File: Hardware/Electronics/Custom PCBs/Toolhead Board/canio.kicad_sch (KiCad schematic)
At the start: 11 parts, among them J1 120TR, J3 CAN, U6 SN65HVD1050D

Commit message: some updates
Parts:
- C18, C19, C22: footprint Capacitor_SMD:C_0402_1005Metric -> (none)
- C23, C24: footprint Capacitor_SMD:C_0402_1005Metric -> (none); LCSC C881999 -> (none)
- CR1: footprint Package_TO_SOT_SMD:SOT-23 -> (none)
- J1: footprint Connector_PinHeader_2.54mm:PinHeader_1x02_P2.54mm_Vertical -> (none)
- J3: footprint Connector_JST:JST_PH_S4B-PH-K_1x04_P2.00mm_Horizontal -> (none)
- R8, R9: footprint Resistor_SMD:R_0402_1005Metric -> (none); LCSC C966873 -> (none)
- U6: footprint Package_SO:SOIC-8_3.9x4.9mm_P1.27mm -> (none)

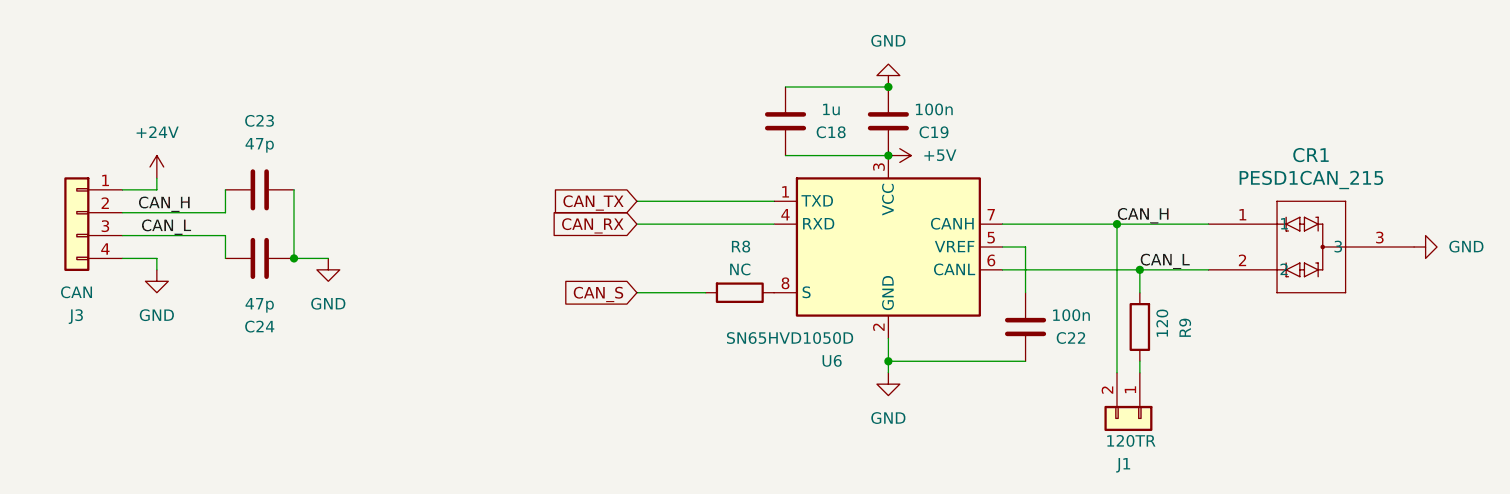
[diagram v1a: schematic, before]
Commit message: Finish Toolhead Schematic
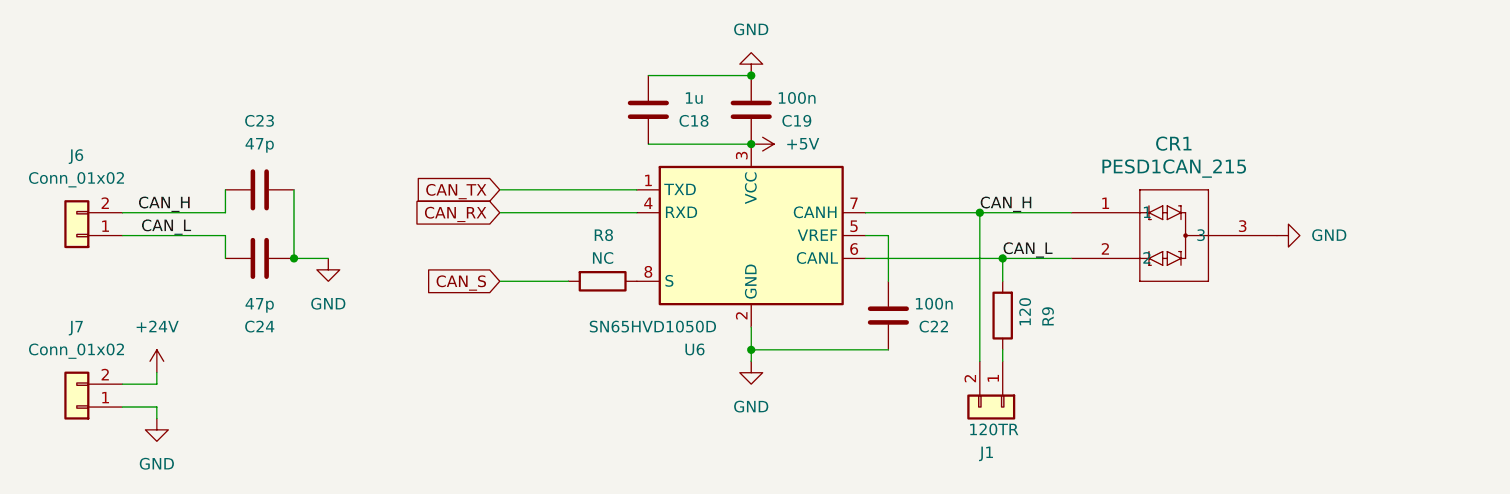
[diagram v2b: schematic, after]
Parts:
- removed J3: CAN, symbol Connector_Generic:Conn_01x04
- added J6, J7: Conn_01x02, symbol Connector_Generic:Conn_01x02
- C18: Digikey (none) -> 1276-1102-1-ND
- C19, C22: Digikey (none) -> 1276-1935-1-ND
- C23, C24: Digikey (none) -> 311-4037-1-ND
- CR1: Digikey (none) -> 5272-PESD1CANCT-ND
- J1: Digikey (none) -> 732-5315-ND
- R8: footprint (none) -> Resistor_SMD:R_0603_1608Metric_Pad0.98x0.95mm_HandSolder
- R9: footprint (none) -> Resistor_SMD:R_0603_1608Metric_Pad0.98x0.95mm_HandSolder; Digikey (none) -> RMCF0603FT120RCT-ND
- U6: Digikey (none) -> 296-19416-5-ND
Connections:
- net +24V: now also J7.2 (Pin_2)
- net CAN_H: now also J6.2 (Pin_2)
- net CAN_L: now also J6.1 (Pin_1)
- net GND: now also J7.1 (Pin_1)
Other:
- moved on the sheet: C18, C19, C22, CR1, J1, R8, R9, U6

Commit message: Updated Footprints
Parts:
- C19: renamed from C18; footprint (none) -> Capacitor_SMD:C_0603_1608Metric_Pad1.08x0.95mm_HandSolder
- C20: renamed from C19; footprint (none) -> Capacitor_SMD:C_0603_1608Metric_Pad1.08x0.95mm_HandSolder
- C23: renamed from C22; footprint (none) -> Capacitor_SMD:C_0603_1608Metric_Pad1.08x0.95mm_HandSolder
- renumbered C23 to C21, C24 to C22, J1 to J8, R8 to R10, R9 to R11, U6 to U5

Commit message: Continue adding footprints
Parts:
- C21, C22: footprint (none) -> Capacitor_SMD:C_0603_1608Metric_Pad1.08x0.95mm_HandSolder
- CR1: footprint (none) -> Package_TO_SOT_SMD:SOT-23
- J6, J7: footprint (none) -> Connector_JST:JST_XH_B2B-XH-AM_1x02_P2.50mm_Vertical
- J8: footprint (none) -> Connector_PinHeader_2.54mm:PinHeader_1x02_P2.54mm_Vertical
- U5: footprint (none) -> Package_SO:SOIC-8_3.9x4.9mm_P1.27mm
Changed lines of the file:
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@@
 			)
 		)
-		(property "Footprint" ""
+		(property "Footprint" "Connector_PinHeader_2.54mm:PinHeader_1x02_P2.54mm_Vertical"
 			(at 130.81 59.69 0)
 			(effects
@@
 			)
 		)
-		(property "Footprint" ""
+		(property "Footprint" "Connector_JST:JST_XH_B2B-XH-AM_1x02_P2.50mm_Vertical"
 			(at 27.94 40.64 0)
 			(effects
@@
 			)
 		)
-		(property "Footprint" ""
+		(property "Footprint" "Capacitor_SMD:C_0603_1608Metric_Pad1.08x0.95mm_HandSolder"
 			(at 52.07 44.1452 0)
 			(effects
@@
 			)
 		)
-		(property "Footprint" ""
+		(property "Footprint" "Package_SO:SOIC-8_3.9x4.9mm_P1.27mm"
 			(at 102.87 53.34 0)
 			(effects
@@
 			)
 		)
-		(property "Footprint" ""
+		(property "Footprint" "Capacitor_SMD:C_0603_1608Metric_Pad1.08x0.95mm_HandSolder"
 			(at 52.07 34.5948 0)
 			(effects
@@
 			)
 		)
-		(property "Footprint" ""
+		(property "Footprint" "Connector_JST:JST_XH_B2B-XH-AM_1x02_P2.50mm_Vertical"
 			(at 27.94 59.69 0)
 			(effects
@@
 			)
 		)
-		(property "Footprint" ""
+		(property "Footprint" "Package_TO_SOT_SMD:SOT-23"
 			(at 138.43 38.1 0)
 			(effects

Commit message: Get basic Toolhead Board outline
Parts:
- renumbered J6 to J10, J7 to J11, J8 to J12
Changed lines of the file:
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@@
 		(on_board yes)
 		(dnp no)
-		(property "Reference" "J8"
+		(property "Reference" "J12"
 			(at 128.27 64.77 90)
 			(effects
@@
 			(project "Toolhead Board"
 				(path "/a1747683-152e-4245-ab61-2d33ce6021ef/ddf7d789-b89f-4838-a0de-61c290d748de"
-					(reference "J8")
+					(reference "J12")
 					(unit 1)
 				)
@@
 		(dnp no)
 		(fields_autoplaced yes)
-		(property "Reference" "J6"
+		(property "Reference" "J10"
 			(at 27.94 31.75 0)
 			(effects
@@
 			(project "Toolhead Board"
 				(path "/a1747683-152e-4245-ab61-2d33ce6021ef/ddf7d789-b89f-4838-a0de-61c290d748de"
-					(reference "J6")
+					(reference "J10")
 					(unit 1)
 				)
@@
 		(dnp no)
 		(fields_autoplaced yes)
-		(property "Reference" "J7"
+		(property "Reference" "J11"
 			(at 27.94 50.8 0)
 			(effects
@@
 			(project "Toolhead Board"
 				(path "/a1747683-152e-4245-ab61-2d33ce6021ef/ddf7d789-b89f-4838-a0de-61c290d748de"
-					(reference "J7")
-					(unit 1)
-				)
+					(reference "J11")
+					(unit 1)
+				)

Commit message: Update layout
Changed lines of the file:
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@@
+	(wire
+		(pts
+			(xy 130.81 43.18) (xy 130.81 45.72)
+		)
+		(stroke
+			(width 0)
+			(type default)
+		)
+	)
+	(wire
+		(pts
+			(xy 44.45 40.64) (xy 33.02 40.64)
+		)
+		(stroke
+			(width 0)
+			(type default)
+		)
+	)
 	(wire
 		(pts
@@
 	(wire
 		(pts
-			(xy 130.81 43.18) (xy 130.81 45.72)
-		)
-		(stroke
-			(width 0)
-			(type default)
-		)
-	)
-	(wire
-		(pts
 			(xy 118.11 40.64) (xy 115.57 40.64)
 		)
@@
 	(wire
 		(pts
-			(xy 33.02 40.64) (xy 44.45 40.64)
-		)
-		(stroke
-			(width 0)
-			(type default)
-		)
-	)
-	(wire
-		(pts
 			(xy 44.45 35.56) (xy 44.45 38.1)
 		)
@@
 		)
 	)
-	(label "CAN_L"
-		(at 40.64 40.64 180)
-		(fields_autoplaced yes)
-		(effects
-			(font
-				(size 1.27 1.27)
-			)
-			(justify right bottom)
-		)
-	)
-	(label "CAN_H"
-		(at 128.27 38.1 0)
-		(fields_autoplaced yes)
-		(effects
-			(font
-				(size 1.27 1.27)
-			)
-			(justify left bottom)
-		)
-	)
-	(label "CAN_H"
-		(at 40.64 38.1 180)
-		(fields_autoplaced yes)
-		(effects
-			(font
-				(size 1.27 1.27)
-			)
-			(justify right bottom)
-		)
-	)
-	(label "CAN_L"
-		(at 130.81 43.18 0)
-		(fields_autoplaced yes)
-		(effects
-			(font
-				(size 1.27 1.27)
-			)
-			(justify left bottom)
+	(global_label "CAN_L"
+		(shape input)
+		(at 44.45 43.18 270)
+		(fields_autoplaced yes)
+		(effects
+			(font
+				(size 1.27 1.27)
+			)
+			(justify right)
+		)
+		(property "Intersheetrefs" "${INTERSHEET_REFS}"
+			(at 44.45 51.85 90)
+			(effects
+				(font
+					(size 1.27 1.27)
+				)
+				(justify right)
+				(hide yes)
+			)
+		)
+	)
+	(global_label "CAN_H"
+		(shape input)
+		(at 138.43 38.1 90)
+		(fields_autoplaced yes)
+		(effects
+			(font
+				(size 1.27 1.27)
+			)
+			(justify left)
+		)
+		(property "Intersheetrefs" "${INTERSHEET_REFS}"
+			(at 138.43 29.1276 90)
+			(effects
+				(font
+					(size 1.27 1.27)
+				)
+				(justify left)
+				(hide yes)
+			)
 		)
 	)
@@
 			(effects
 				(font
+					(size 1.27 1.27)
+				)
+				(justify right)
+				(hide yes)
+			)
+		)
+	)
+	(global_label "CAN_H"
+		(shape input)
+		(at 44.45 35.56 90)
+		(fields_autoplaced yes)
+		(effects
+			(font
+				(size 1.27 1.27)
+			)
+			(justify left)
+		)
+		(property "Intersheetrefs" "${INTERSHEET_REFS}"
+			(at 44.45 26.5876 90)
+			(effects
+				(font
+					(size 1.27 1.27)
+				)
+				(justify left)
+				(hide yes)
+			)
+		)
+	)
+	(global_label "CAN_L"
+		(shape input)
+		(at 138.43 43.18 270)
+		(fields_autoplaced yes)
+		(effects
+			(font
+				(size 1.27 1.27)
+			)
+			(justify right)
+		)
+		(property "Intersheetrefs" "${INTERSHEET_REFS}"
+			(at 138.43 51.85 90)
+			(effects
+				(font

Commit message: Update toolhead board yet again
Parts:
- renumbered J10 to J7, J11 to J8, J12 to J9
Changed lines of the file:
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@@
 		(on_board yes)
 		(dnp no)
-		(property "Reference" "J12"
+		(property "Reference" "J9"
 			(at 128.27 64.77 90)
 			(effects
@@
 			(project "Toolhead Board"
 				(path "/a1747683-152e-4245-ab61-2d33ce6021ef/ddf7d789-b89f-4838-a0de-61c290d748de"
-					(reference "J12")
+					(reference "J9")
 					(unit 1)
 				)
@@
 		(dnp no)
 		(fields_autoplaced yes)
-		(property "Reference" "#PWR053"
+		(property "Reference" "#PWR052"
 			(at 36.83 59.69 0)
 			(effects
@@
 			(project "Toolhead Board"
 				(path "/a1747683-152e-4245-ab61-2d33ce6021ef/ddf7d789-b89f-4838-a0de-61c290d748de"
-					(reference "#PWR053")
+					(reference "#PWR052")
 					(unit 1)
 				)
@@
 		(dnp no)
 		(fields_autoplaced yes)
-		(property "Reference" "#PWR051"
+		(property "Reference" "#PWR050"
 			(at 55.88 49.53 0)
 			(effects
@@
 			(project "Toolhead Board"
 				(path "/a1747683-152e-4245-ab61-2d33ce6021ef/ddf7d789-b89f-4838-a0de-61c290d748de"
-					(reference "#PWR051")
+					(reference "#PWR050")
 					(unit 1)
 				)
@@
 		(dnp no)
 		(fields_autoplaced yes)
-		(property "Reference" "J10"
+		(property "Reference" "J7"
 			(at 27.94 31.75 0)
 			(effects
@@
 			(project "Toolhead Board"
 				(path "/a1747683-152e-4245-ab61-2d33ce6021ef/ddf7d789-b89f-4838-a0de-61c290d748de"
-					(reference "J10")
+					(reference "J7")
 					(unit 1)
 				)
@@
 		(dnp no)
 		(fields_autoplaced yes)
-		(property "Reference" "#PWR054"
+		(property "Reference" "#PWR053"
 			(at 36.83 67.31 0)
 			(effects
@@
 			(project "Toolhead Board"
 				(path "/a1747683-152e-4245-ab61-2d33ce6021ef/ddf7d789-b89f-4838-a0de-61c290d748de"
-					(reference "#PWR054")
+					(reference "#PWR053")
 					(unit 1)
 				)
@@
 		(dnp no)
 		(fields_autoplaced yes)
-		(property "Reference" "#PWR050"
+		(property "Reference" "#PWR049"
 			(at 167.64 40.64 0)
 			(effects
@@
 			(project "Toolhead Board"
 				(path "/a1747683-152e-4245-ab61-2d33ce6021ef/ddf7d789-b89f-4838-a0de-61c290d748de"
-					(reference "#PWR050")
+					(reference "#PWR049")
 					(unit 1)
 				)
@@
 		(dnp no)
 		(fields_autoplaced yes)
-		(property "Reference" "#PWR049"
+		(property "Reference" "#PWR048"
 			(at 99.06 30.48 0)
 			(effects
@@
 			(project "Toolhead Board"
 				(path "/a1747683-152e-4245-ab61-2d33ce6021ef/ddf7d789-b89f-4838-a0de-61c290d748de"
-					(reference "#PWR049")
+					(reference "#PWR048")
 					(unit 1)
 				)
@@
 		(dnp no)
 		(fields_autoplaced yes)
-		(property "Reference" "#PWR052"
+		(property "Reference" "#PWR051"
 			(at 102.87 60.96 0)
 			(effects
@@
 			(project "Toolhead Board"
 				(path "/a1747683-152e-4245-ab61-2d33ce6021ef/ddf7d789-b89f-4838-a0de-61c290d748de"
-					(reference "#PWR052")
+					(reference "#PWR051")
 					(unit 1)
 				)
@@
 		(dnp no)
 		(fields_autoplaced yes)
-		(property "Reference" "#PWR048"
+		(property "Reference" "#PWR047"
 			(at 102.87 16.51 0)
 			(effects
@@
 			(project "Toolhead Board"
 				(path "/a1747683-152e-4245-ab61-2d33ce6021ef/ddf7d789-b89f-4838-a0de-61c290d748de"
-					(reference "#PWR048")
+					(reference "#PWR047")
 					(unit 1)
 				)
@@
 		(dnp no)
 		(fields_autoplaced yes)
-		(property "Reference" "J11"
+		(property "Reference" "J8"
 			(at 27.94 50.8 0)
 			(effects
@@
 			(project "Toolhead Board"
 				(path "/a1747683-152e-4245-ab61-2d33ce6021ef/ddf7d789-b89f-4838-a0de-61c290d748de"
-					(reference "J11")
-					(unit 1)
-				)
+					(reference "J8")
+					(unit 1)
+				)

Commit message: Update layout slightly
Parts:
- J7: footprint Connector_JST:JST_XH_B2B-XH-AM_1x02_P2.50mm_Vertical -> Connector_JST:JST_PH_B2B-PH-K_1x02_P2.00mm_Vertical
- J8: footprint Connector_JST:JST_XH_B2B-XH-AM_1x02_P2.50mm_Vertical -> Connector_AMASS:AMASS_XT30U-F_1x02_P5.0mm_Vertical
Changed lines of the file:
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@@
 			)
 		)
-		(property "Footprint" "Connector_JST:JST_XH_B2B-XH-AM_1x02_P2.50mm_Vertical"
+		(property "Footprint" "Connector_JST:JST_PH_B2B-PH-K_1x02_P2.00mm_Vertical"
 			(at 27.94 40.64 0)
 			(effects
@@
 			)
 		)
-		(property "Footprint" "Connector_JST:JST_XH_B2B-XH-AM_1x02_P2.50mm_Vertical"
+		(property "Footprint" "Connector_AMASS:AMASS_XT30U-F_1x02_P5.0mm_Vertical"
 			(at 27.94 59.69 0)
 			(effects
